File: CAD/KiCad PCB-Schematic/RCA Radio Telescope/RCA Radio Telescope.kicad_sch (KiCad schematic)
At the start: 16 parts, among them J2 USB_B_MICRO, J3 5V In For Filter Board, J6 3V Out For LNA, J7 Input from SDR, J8 5V Out For Filter Board, J9 5V From PoE Splitter, U1 ZX60-P33ULN+, U2 ADALM Pluto SDR

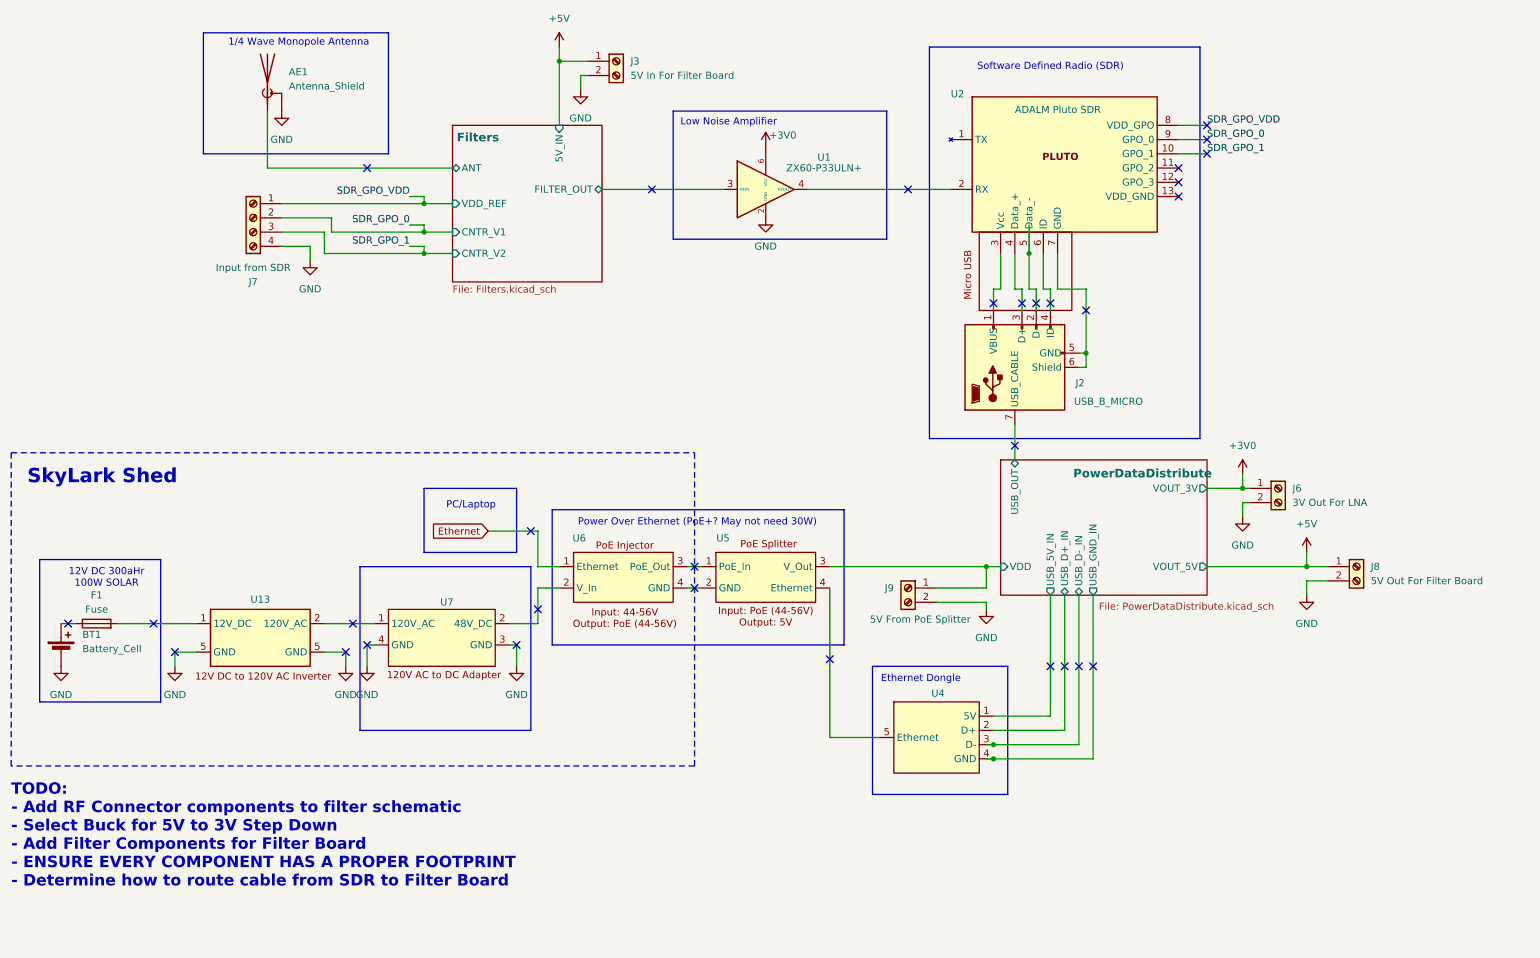
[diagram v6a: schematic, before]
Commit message: Updated Schematic
Updated Root Schematic to v1.5, Filters to v1.1, and PowerDataDistribute to v1.1.
- Updated part references to be more consistent
- Added missing GND label for SDR GPO
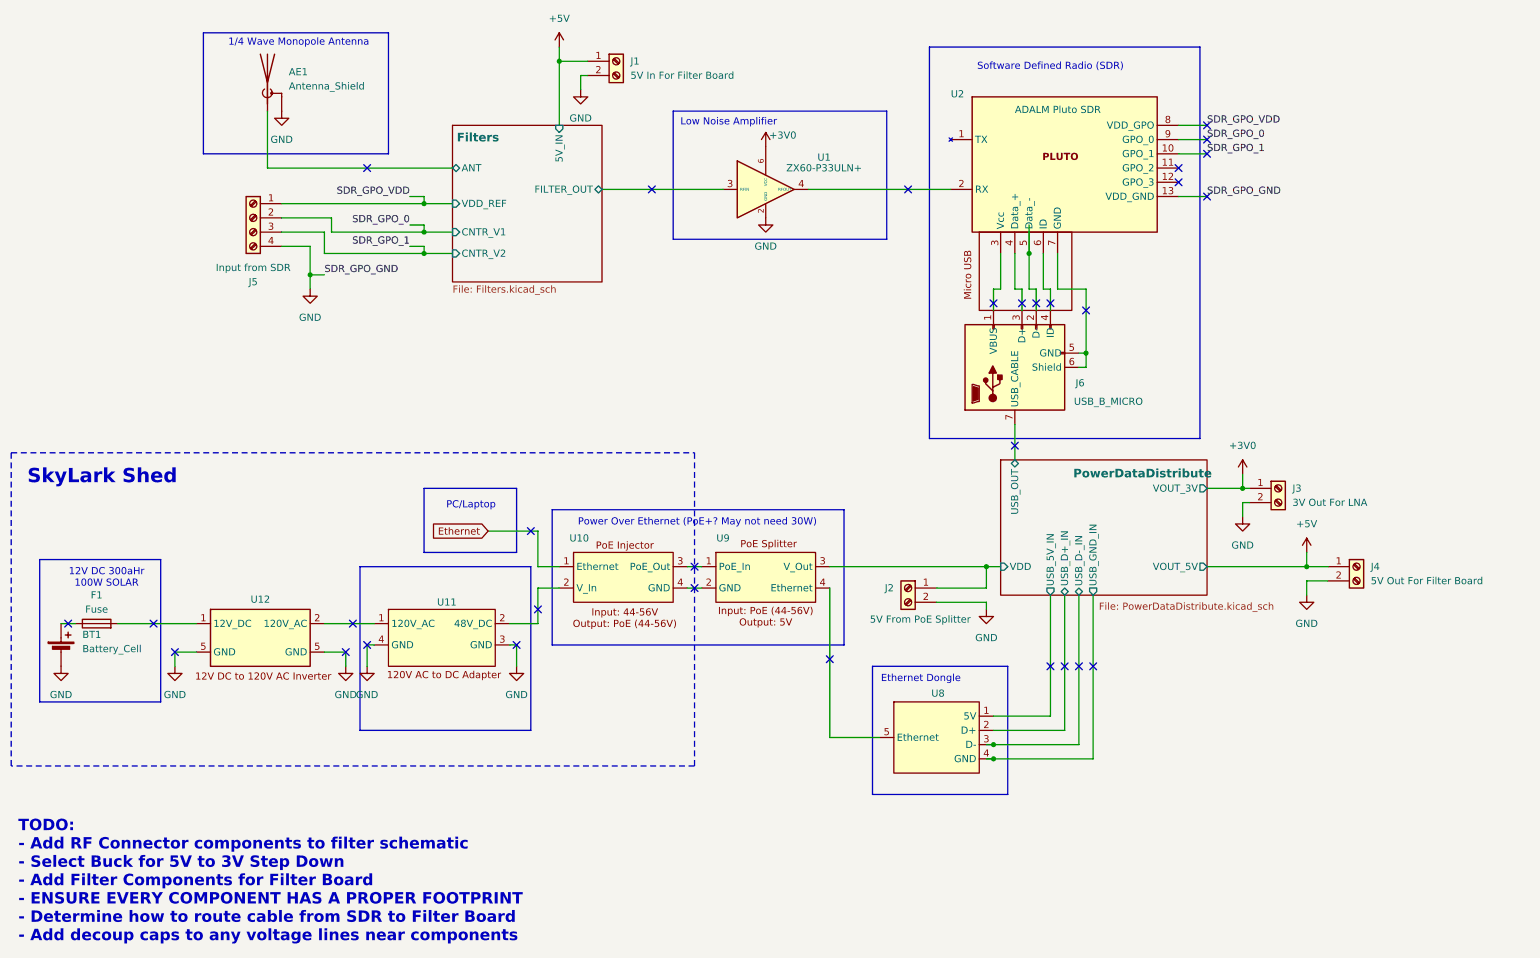
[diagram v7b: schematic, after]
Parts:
- renumbered J3 to J1, J9 to J2, J6 to J3, J8 to J4, J7 to J5, J2 to J6, U6 to U10, U7 to U11, U13 to U12, U4 to U8, U5 to U9
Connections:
- net GND: now also U2.13 (VDD_GND)
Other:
- note added: "TODO: - Add RF Connector components to filter schematic - Select Buck for 5V to 3V Step Down - Add Filter Components for Filter Board - ENSURE EVERY COMPONENT HAS A PROPER FOOTPRINT - Determine how to route cable from SDR to Filter Board - Add decoup caps to any voltage lines near components"
- note removed: "TODO: - Add RF Connector components to filter schematic - Select Buck for 5V to 3V Step Down - Add Filter Components for Filter Board - ENSURE EVERY COMPONENT HAS A PROPER FOOTPRINT - Determine how to route cable from SDR to Filter Board"
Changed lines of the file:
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@@
 		(title "RCA Radio Telescope System")
 		(date "2025-02-09")
-		(rev "Version 1.4")
+		(rev "Version 1.5")
 	)
 	(junction
@@
 	)
 	(junction
+		(at 68.58 60.96)
+		(diameter 0)
+		(color 0 0 0 0)
+	)
+	(junction
 		(at 190.5 147.32)
 		(diameter 0)
@@
 	)
 	(no_connect
-		(at 223.52 46.99)
+		(at 228.6 46.99)
 	)
 	(no_connect
@@
 	(wire
 		(pts
-			(xy 68.58 55.88) (xy 68.58 58.42)
+			(xy 68.58 55.88) (xy 68.58 60.96)
 		)
 		(stroke
@@
 	(wire
 		(pts
+			(xy 68.58 60.96) (xy 71.12 60.96)
+		)
+		(stroke
+			(width 0)
+			(type default)
+		)
+	)
+	(wire
+		(pts
 			(xy 196.85 57.15) (xy 196.85 63.5)
 		)
@@
 	(wire
 		(pts
+			(xy 68.58 60.96) (xy 68.58 63.5)
+		)
+		(stroke
+			(width 0)
+			(type default)
+		)
+	)
+	(wire
+		(pts
 			(xy 135.89 116.84) (xy 138.43 116.84)
 		)
@@
 	(wire
 		(pts
+			(xy 228.6 46.99) (xy 223.52 46.99)
+		)
+		(stroke
+			(width 0)
+			(type default)
+		)
+	)
+	(wire
+		(pts
 			(xy 161.29 113.03) (xy 189.23 113.03)
 		)
@@
 		)
 	)
-	(text "TODO:\n- Add RF Connector components to filter schematic\n- Select Buck for 5V to 3V Step Down\n- Add Filter Components for Filter Board\n- ENSURE EVERY COMPONENT HAS A PROPER FOOTPRINT\n- Determine how to route cable from SDR to Filter Board"
+	(text "TODO:\n- Add RF Connector components to filter schematic\n- Select Buck for 5V to 3V Step Down\n- Add Filter Components for Filter Board\n- ENSURE EVERY COMPONENT HAS A PROPER FOOTPRINT\n- Determine how to route cable from SDR to Filter Board\n- Add decoup caps to any voltage lines near components"
 		(exclude_from_sim no)
-		(at 15.24 161.036 0)
+		(at 16.51 169.164 0)
 		(effects
 			(font
@@
 		)
 	)
+	(label "SDR_GPO_GND"
+		(at 228.6 46.99 0)
+		(effects
+			(font
+				(size 1.27 1.27)
+			)
+			(justify left bottom)
+		)
+	)
 	(label "SDR_GPO_1"
 		(at 228.6 39.37 0)
@@
 		)
 	)
+	(label "SDR_GPO_GND"
+		(at 71.12 60.96 0)
+		(effects
+			(font
+				(size 1.27 1.27)
+			)
+			(justify left bottom)
+		)
+	)
 	(label "SDR_GPO_VDD"
 		(at 228.6 34.29 0)
@@
 		(on_board yes)
 		(dnp no)
-		(property "Reference" "J9"
+		(property "Reference" "J2"
 			(at 172.72 116.8399 0)
 			(effects
@@
 			(project "RCA Radio Telescope"
 				(path "/1630c5ee-b70a-455e-85ba-86a73955b8fd"
-					(reference "J9")
+					(reference "J2")
 					(unit 1)
 				)
@@
 		(on_board yes)
 		(dnp no)
-		(property "Reference" "U5"
+		(property "Reference" "U9"
 			(at 142.24 107.95 0)
 			(effects
@@
 			(project ""
 				(path "/1630c5ee-b70a-455e-85ba-86a73955b8fd"
-					(reference "U5")
+					(reference "U9")
 					(unit 1)
 				)
@@
 		(dnp no)
 		(fields_autoplaced yes)
-		(property "Reference" "J6"
+		(property "Reference" "J3"
 			(at 243.84 99.0599 0)
 			(effects
@@
 			(project "RCA Radio Telescope"
 				(path "/1630c5ee-b70a-455e-85ba-86a73955b8fd"
-					(reference "J6")
+					(reference "J3")
 					(unit 1)
 				)
@@
 		(dnp no)
 		(fields_autoplaced yes)
-		(property "Reference" "J8"
+		(property "Reference" "J4"
 			(at 257.81 113.0299 0)
 			(effects
@@
 			(project "RCA Radio Telescope"
 				(path "/1630c5ee-b70a-455e-85ba-86a73955b8fd"
-					(reference "J8")
+					(reference "J4")
 					(unit 1)
 				)
@@
 	(symbol
 		(lib_id "power:GND")
-		(at 68.58 58.42 0)
+		(at 68.58 63.5 0)
 		(unit 1)
 		(exclude_from_sim no)
@@
 		(fields_autoplaced yes)
 		(property "Reference" "#PWR029"
-			(at 68.58 64.77 0)
+			(at 68.58 69.85 0)
 			(effects
 				(font
@@
 		)
 		(property "Value" "GND"
-			(at 68.58 63.5 0)
+			(at 68.58 68.58 0)
 			(effects
 				(font
@@
 		)
 		(property "Footprint" ""
-			(at 68.58 58.42 0)
+			(at 68.58 63.5 0)
 			(effects
 				(font
@@
 		)
 		(property "Datasheet" ""
-			(at 68.58 58.42 0)
+			(at 68.58 63.5 0)
 			(effects
 				(font
@@
 		)
 		(property "Description" "Power symbol creates a global label with name \"GND\" , ground"
-			(at 68.58 58.42 0)
+			(at 68.58 63.5 0)
 			(effects
 				(font
@@
 		(on_board yes)
 		(dnp no)
-		(property "Reference" "J2"
+		(property "Reference" "J6"
 			(at 206.756 80.264 90)
 			(effects
@@
 			(project ""
 				(path "/1630c5ee-b70a-455e-85ba-86a73955b8fd"
-					(reference "J2")
+					(reference "J6")
 					(unit 1)
 				)
@@
 		(on_board yes)
 		(dnp no)
-		(property "Reference" "U13"
+		(property "Reference" "U12"
 			(at 59.69 118.872 0)
 			(effects
@@
 			(project ""
 				(path "/1630c5ee-b70a-455e-85ba-86a73955b8fd"
-					(reference "U13")
+					(reference "U12")
 					(unit 1)
 				)
@@
 		(dnp no)
 		(fields_autoplaced yes)
-		(property "Reference" "J3"
+		(property "Reference" "J1"
 			(at 125.73 22.8599 0)
 			(effects
@@
 			(project "RCA Radio Telescope"
 				(path "/1630c5ee-b70a-455e-85ba-86a73955b8fd"
-					(reference "J3")
+					(reference "J1")
 					(unit 1)
 				)
@@
 		(on_board yes)
 		(dnp no)
-		(property "Reference" "U6"
+		(property "Reference" "U10"
 			(at 116.586 107.95 0)
 			(effects
@@
 			(project ""
 				(path "/1630c5ee-b70a-455e-85ba-86a73955b8fd"
-					(reference "U6")
+					(reference "U10")
 					(unit 1)
 				)
@@
 		(on_board yes)
 		(dnp no)
-		(property "Reference" "J7"
+		(property "Reference" "J5"
 			(at 58.42 62.23 0)
 			(effects
@@
 			(project "RCA Radio Telescope"
 				(path "/1630c5ee-b70a-455e-85ba-86a73955b8fd"
-					(reference "J7")
+					(reference "J5")
 					(unit 1)
 				)
@@
 		(on_board yes)
 		(dnp no)
-		(property "Reference" "U4"
+		(property "Reference" "U8"
 			(at 180.594 135.636 0)
 			(effects
@@
 			(project ""
 				(path "/1630c5ee-b70a-455e-85ba-86a73955b8fd"
-					(reference "U4")
+					(reference "U8")
 					(unit 1)
 				)
@@
 		(on_board yes)
 		(dnp no)
-		(property "Reference" "U7"
+		(property "Reference" "U11"
 			(at 92.964 119.38 0)
 			(effects
@@
 			(project ""
 				(path "/1630c5ee-b70a-455e-85ba-86a73955b8fd"
-					(reference "U7")
+					(reference "U11")
 					(unit 1)
 				)

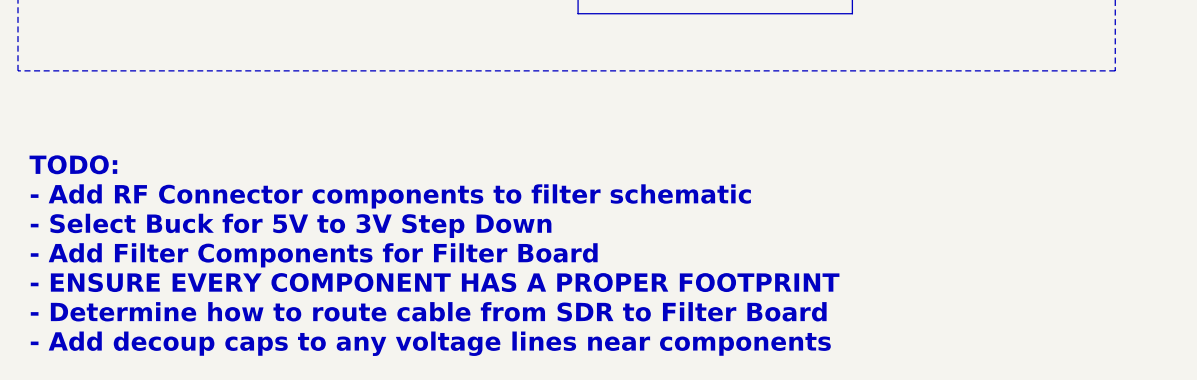
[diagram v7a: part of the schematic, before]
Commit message: Updated PowerDataDistribute Schematic to v1.3
- Added 5V to 3V Buck for LNA
- Added TVS diode, PMOS, and polyfuse for power protection (need to select PMOS and polyfuse)
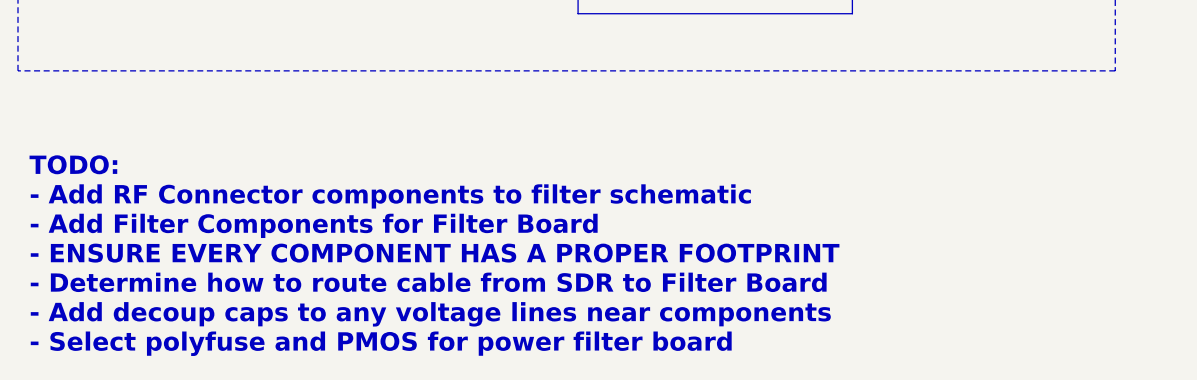
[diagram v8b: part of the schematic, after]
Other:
- note added: "TODO: - Add RF Connector components to filter schematic - Add Filter Components for Filter Board - ENSURE EVERY COMPONENT HAS A PROPER FOOTPRINT - Determine how to route cable from SDR to Filter Board - Add decoup caps to any voltage lines near components - Select polyfuse and PMOS for power filter board"
- note removed: "TODO: - Add RF Connector components to filter schematic - Select Buck for 5V to 3V Step Down - Add Filter Components for Filter Board - ENSURE EVERY COMPONENT HAS A PROPER FOOTPRINT - Determine how to route cable from SDR to Filter Board - Add decoup caps to any voltage lines near components"
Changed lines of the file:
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@@
 		)
 	)
-	(text "TODO:\n- Add RF Connector components to filter schematic\n- Select Buck for 5V to 3V Step Down\n- Add Filter Components for Filter Board\n- ENSURE EVERY COMPONENT HAS A PROPER FOOTPRINT\n- Determine how to route cable from SDR to Filter Board\n- Add decoup caps to any voltage lines near components"
+	(text "TODO:\n- Add RF Connector components to filter schematic\n- Add Filter Components for Filter Board\n- ENSURE EVERY COMPONENT HAS A PROPER FOOTPRINT\n- Determine how to route cable from SDR to Filter Board\n- Add decoup caps to any voltage lines near components\n- Select polyfuse and PMOS for power filter board"
 		(exclude_from_sim no)
 		(at 16.51 169.164 0)
@@
 	(label "SDR_GPO_0"
 		(at 228.6 36.83 0)
+		(fields_autoplaced yes)
 		(effects
 			(font
@@
 	(label "SDR_GPO_GND"
 		(at 228.6 46.99 0)
+		(fields_autoplaced yes)
 		(effects
 			(font
@@
 	(label "SDR_GPO_1"
 		(at 228.6 39.37 0)
+		(fields_autoplaced yes)
 		(effects
 			(font
@@
 	(label "SDR_GPO_GND"
 		(at 71.12 60.96 0)
+		(fields_autoplaced yes)
 		(effects
 			(font
@@
 	(label "SDR_GPO_VDD"
 		(at 228.6 34.29 0)
+		(fields_autoplaced yes)
 		(effects
 			(font
@@
 	(label "SDR_GPO_1"
 		(at 86.36 55.88 180)
+		(fields_autoplaced yes)
 		(effects
 			(font
@@
 	(label "SDR_GPO_VDD"
 		(at 86.36 46.99 180)
+		(fields_autoplaced yes)
 		(effects
 			(font
@@
 	(label "SDR_GPO_0"
 		(at 86.36 52.07 180)
+		(fields_autoplaced yes)
 		(effects
 			(font
